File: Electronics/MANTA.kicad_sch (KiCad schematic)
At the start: 33 parts, among them U2 Ai-Thinker-Ra-02

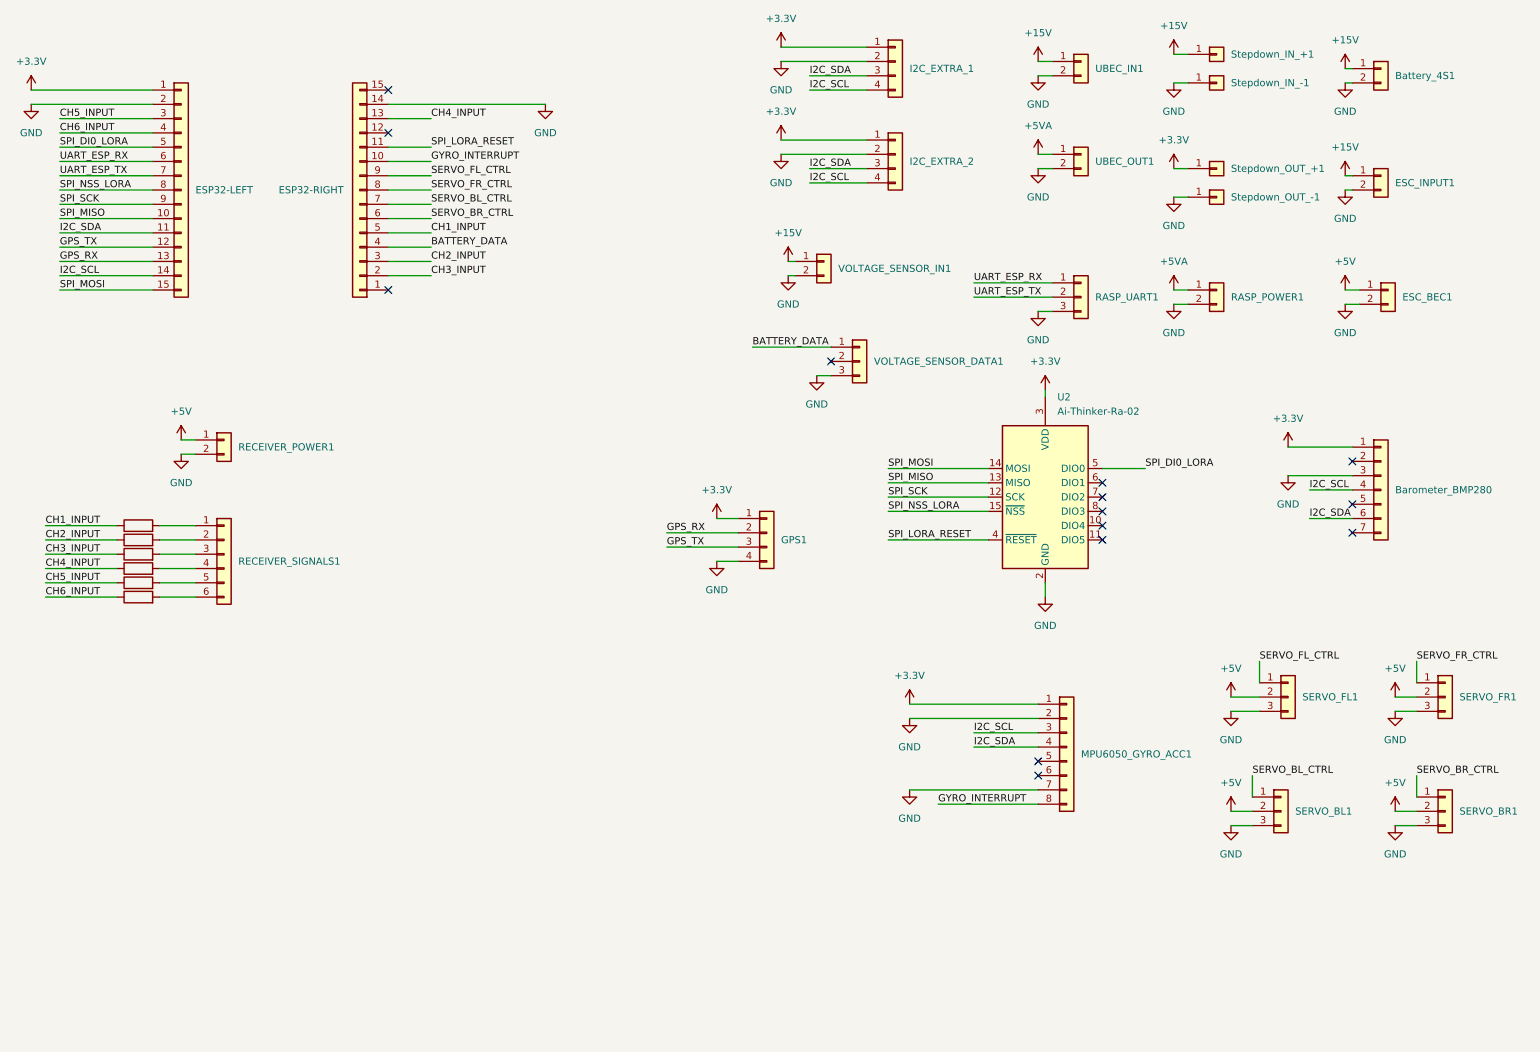
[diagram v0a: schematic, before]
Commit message: Update electronics for hardware compatibility
- Updated the schematic and KiCad project to align with the physical hardware purchased.
- Replaced generic connectors with specific 2.54mm pitch vertical pin headers (1x07 and 1x02) for the ESP32 and power distribution modules.
- Refactored power routing and replaced symbols (adjusting GND, +15V, and +5V).
- Updated designators (e.g., ESP32-LEFT1, ESP32-RIGHT1, EXTRA_ENERGY_15V1) to correctly match the interfaces of the new physical components.
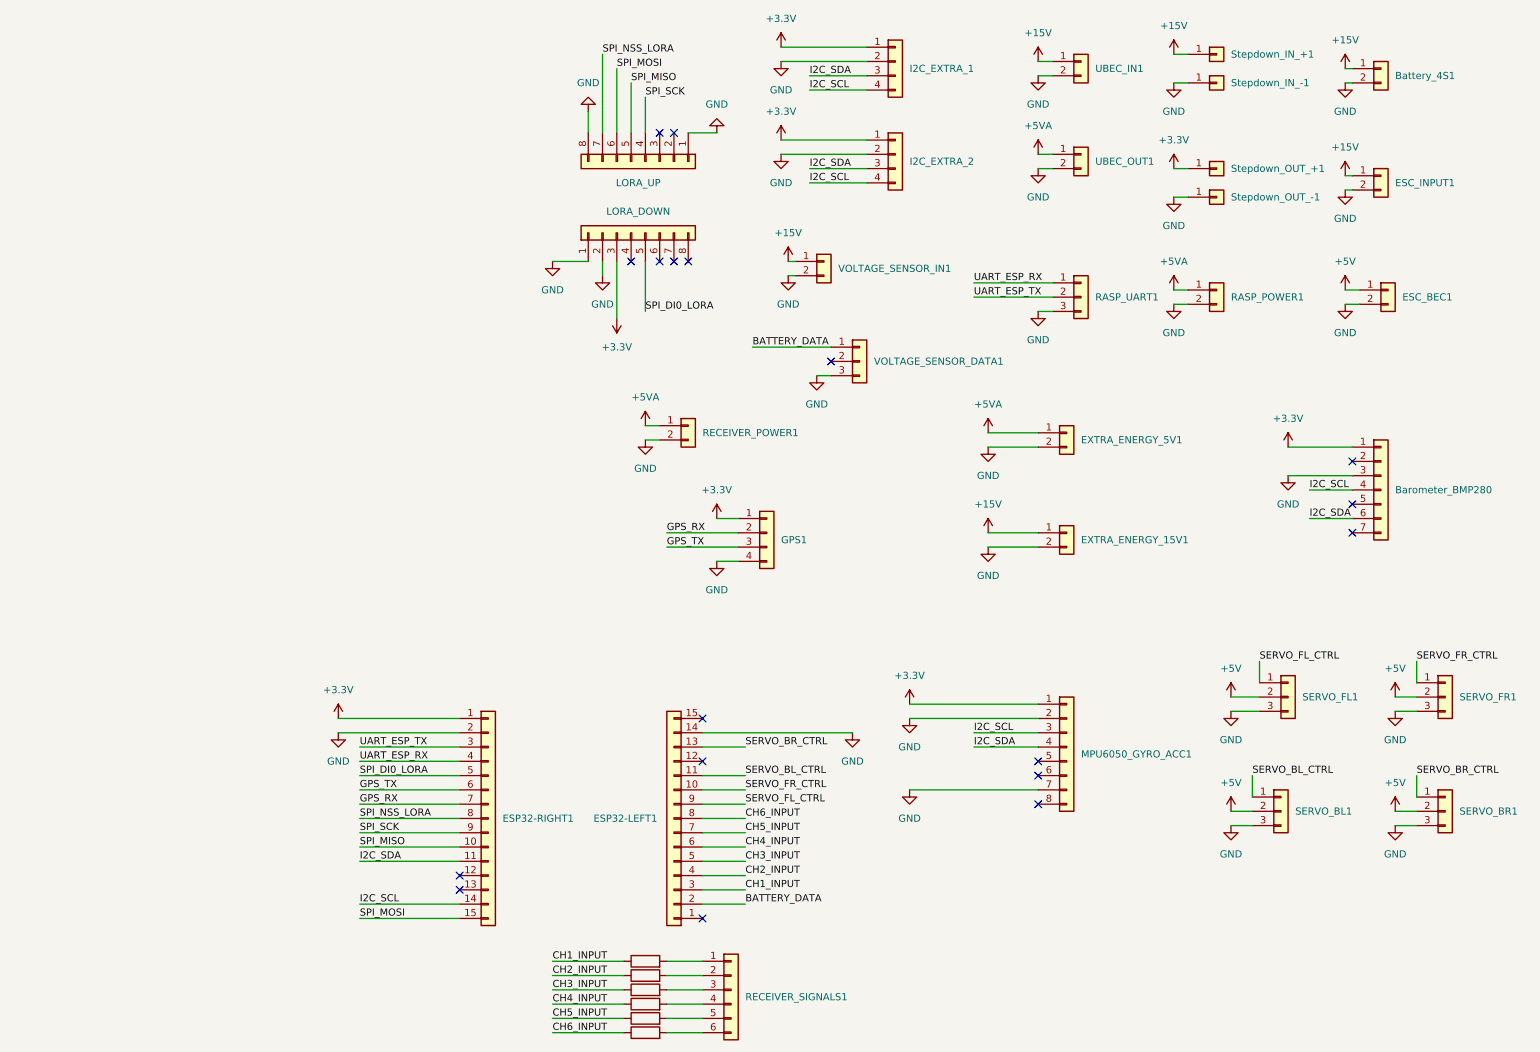
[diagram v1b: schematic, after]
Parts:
- removed U2: Ai-Thinker-Ra-02, symbol RF_Module:Ai-Thinker-Ra-02
- added EXTRA_ENERGY_15V1, EXTRA_ENERGY_5V1: Conn_01x02, symbol Connector_Generic:Conn_01x02
- added J1: LORA_UP, Connector_PinHeader_2.54mm:PinHeader_1x08_P2.54mm_Vertical, symbol Connector_Generic:Conn_01x08
- added J2: LORA_DOWN, Connector_PinHeader_2.54mm:PinHeader_1x08_P2.54mm_Vertical, symbol Connector_Generic:Conn_01x08
- Barometer_BMP280: footprint (none) -> Connector_PinHeader_2.54mm:PinHeader_1x07_P2.54mm_Vertical
- Battery_4S1, ESC_INPUT1, VOLTAGE_SENSOR_IN1: footprint (none) -> Connector_Wire:SolderWire-6sqmm_1x02_P14mm_D3.5mm_OD7mm
- ESC_BEC1, RASP_POWER1, RECEIVER_POWER1, UBEC_IN1, UBEC_OUT1: footprint (none) -> Connector_PinHeader_2.54mm:PinHeader_1x02_P2.54mm_Vertical
- ESP32-LEFT1: renamed from ESP32-RIGHT; footprint (none) -> Connector_PinHeader_2.54mm:PinHeader_1x15_P2.54mm_Vertical
- ESP32-RIGHT1: renamed from ESP32-LEFT; footprint (none) -> Connector_PinHeader_2.54mm:PinHeader_1x15_P2.54mm_Vertical
- GPS1, I2C_EXTRA_1, I2C_EXTRA_2: footprint (none) -> Connector_PinHeader_2.54mm:PinHeader_1x04_P2.54mm_Vertical
- MPU6050_GYRO_ACC1: footprint (none) -> Connector_PinHeader_2.54mm:PinHeader_1x08_P2.54mm_Vertical
- R1, R2, R3, R4, R5, R6: footprint (none) -> Resistor_THT:R_Axial_DIN0207_L6.3mm_D2.5mm_P10.16mm_Horizontal
- RASP_UART1, SERVO_BL1, SERVO_BR1, SERVO_FL1, SERVO_FR1, VOLTAGE_SENSOR_DATA1: footprint (none) -> Connector_PinHeader_2.54mm:PinHeader_1x03_P2.54mm_Vertical
- RECEIVER_SIGNALS1: footprint (none) -> Connector_PinHeader_2.54mm:PinHeader_1x06_P2.54mm_Vertical
- Stepdown_IN_+1, Stepdown_IN_-1, Stepdown_OUT_+1, Stepdown_OUT_-1: footprint (none) -> Connector_PinHeader_2.54mm:PinHeader_1x01_P2.54mm_Vertical
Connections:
- net SPI_LORA_RESET is gone; now on net SERVO_BL_CTRL: ESP32-LEFT1.11 (Pin_11)
- net +15V: now also EXTRA_ENERGY_15V1.1 (Pin_1)
- net +3.3V: now also J2.3 (Pin_3)
- net +5V: no longer RECEIVER_POWER1.1 (Pin_1)
- net +5VA: now also RECEIVER_POWER1.1 (Pin_1), EXTRA_ENERGY_5V1.1 (Pin_1)
- net BATTERY_DATA: now also ESP32-LEFT1.2 (Pin_2); no longer ESP32-LEFT1.4 (Pin_4)
- net CH1_INPUT: now also ESP32-LEFT1.3 (Pin_3); no longer ESP32-LEFT1.5 (Pin_5)
- net CH2_INPUT: now also ESP32-LEFT1.4 (Pin_4); no longer ESP32-LEFT1.3 (Pin_3)
- net CH3_INPUT: now also ESP32-LEFT1.5 (Pin_5); no longer ESP32-LEFT1.2 (Pin_2)
- net CH4_INPUT: now also ESP32-LEFT1.6 (Pin_6); no longer ESP32-LEFT1.13 (Pin_13)
- net CH5_INPUT: now also ESP32-LEFT1.7 (Pin_7); no longer ESP32-RIGHT1.3 (Pin_3)
- net CH6_INPUT: now also ESP32-LEFT1.8 (Pin_8); no longer ESP32-RIGHT1.4 (Pin_4)
- net GND: now also EXTRA_ENERGY_15V1.2 (Pin_2), EXTRA_ENERGY_5V1.2 (Pin_2), J1.1 (Pin_1), J1.8 (Pin_8), J2.1 (Pin_1), J2.2 (Pin_2)
- net GPS_RX: now also ESP32-RIGHT1.7 (Pin_7); no longer ESP32-RIGHT1.13 (Pin_13)
- net GPS_TX: now also ESP32-RIGHT1.6 (Pin_6); no longer ESP32-RIGHT1.12 (Pin_12)
- net SERVO_BL_CTRL: no longer ESP32-LEFT1.7 (Pin_7)
- net SERVO_BR_CTRL: now also ESP32-LEFT1.13 (Pin_13); no longer ESP32-LEFT1.6 (Pin_6)
- net SERVO_FR_CTRL: now also ESP32-LEFT1.10 (Pin_10); no longer ESP32-LEFT1.8 (Pin_8)
- net SPI_DI0_LORA: now also J2.5 (Pin_5)
- net SPI_MISO: now also J1.5 (Pin_5)
- net SPI_MOSI: now also J1.6 (Pin_6)
- net SPI_NSS_LORA: now also J1.7 (Pin_7)
- net SPI_SCK: now also J1.4 (Pin_4)
- net UART_ESP_RX: now also ESP32-RIGHT1.4 (Pin_4); no longer ESP32-RIGHT1.6 (Pin_6)
- net UART_ESP_TX: now also ESP32-RIGHT1.3 (Pin_3); no longer ESP32-RIGHT1.7 (Pin_7)
- net GYRO_INTERRUPT: no longer names the net of MPU6050_GYRO_ACC1.8 (Pin_8)
- net GYRO_INTERRUPT: no longer ESP32-LEFT1.10 (Pin_10)
- no-connect marks 14 -> 18
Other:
- moved on the sheet: ESP32-LEFT1, ESP32-RIGHT1, RECEIVER_POWER1, RECEIVER_SIGNALS1

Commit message: Update electronics schematic
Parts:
- EXTRA_ENERGY_15V1, EXTRA_ENERGY_5V1: footprint (none) -> Connector_PinHeader_2.54mm:PinHeader_1x02_P2.54mm_Vertical
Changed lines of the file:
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@@
 			)
 		)
-		(property "Footprint" ""
+		(property "Footprint" "Connector_PinHeader_2.54mm:PinHeader_1x02_P2.54mm_Vertical"
 			(at 204.47 88.9 0)
 			(hide yes)
@@
 			)
 		)
-		(property "Footprint" ""
+		(property "Footprint" "Connector_PinHeader_2.54mm:PinHeader_1x02_P2.54mm_Vertical"
 			(at 204.47 106.68 0)
 			(hide yes)
